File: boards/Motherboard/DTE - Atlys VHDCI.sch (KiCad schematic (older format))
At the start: 3 parts, among them J201 DIGILENT_VHDCI_CONN

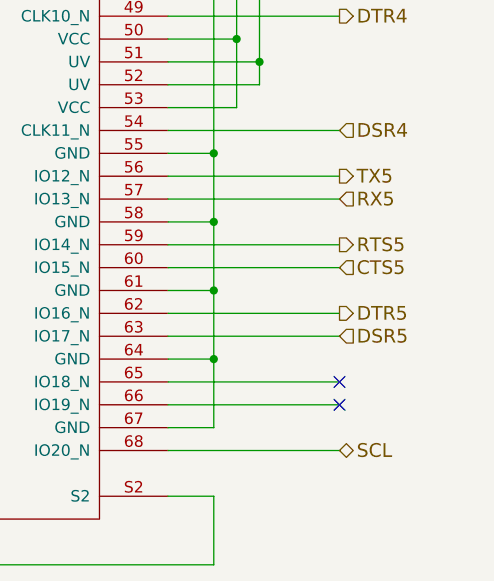
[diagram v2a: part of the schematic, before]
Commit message: Change to 5 serial port; Connect Atlys and PIC18F SPI; Entire schematic updated
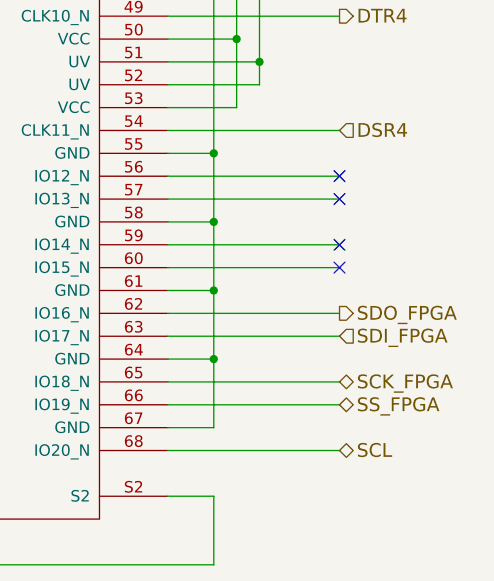
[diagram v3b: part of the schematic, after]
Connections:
- net SCK_FPGA: now reaches J201.65 (IO18_N)
- net SS_FPGA: now reaches J201.66 (IO19_N)
- net CTS5: no longer names the net of J201.60 (IO15_N)
- net DSR5 renamed SDI_FPGA
- net DTR5 renamed SDO_FPGA
- net RTS5: no longer names the net of J201.59 (IO14_N)
- net RX5: no longer names the net of J201.57 (IO13_N)
- net TX5: no longer names the net of J201.56 (IO12_N)
- no-connect marks 2 -> 4
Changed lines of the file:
@@
 Sheet 2 7
 Title ""
-Date "26 jun 2014"
+Date "30 jun 2014"
 Rev ""
 Comp "TimVideos"
@@
 Text HLabel 7350 4150 2    60   Input ~ 0
 DSR4
-Text HLabel 7350 4350 2    60   Output ~ 0
-TX5
-Text HLabel 7350 4650 2    60   Output ~ 0
-RTS5
-Text HLabel 7350 4950 2    60   Output ~ 0
-DTR5
 Text HLabel 7350 5550 2    60   BiDi ~ 0
 SCL
 Text HLabel 7350 2450 2    60   Output ~ 0
 RTS3
-Text HLabel 7350 4450 2    60   Input ~ 0
-RX5
-Text HLabel 7350 4750 2    60   Input ~ 0
-CTS5
-Text HLabel 7350 5050 2    60   Input ~ 0
-DSR5
-NoConn ~ 7350 5250
-NoConn ~ 7350 5350
 Wire Wire Line
 	6800 6050 6800 5750
@@
 Connection ~ 3750 6050
 $Comp
-L PWR_FLAG #FLG201
+L PWR_FLAG #FLG01
 U 1 1 53C07D98
 P 3750 5450
-F 0 "#FLG201" H 3750 5545 30  0001 C CNN
+F 0 "#FLG01" H 3750 5545 30  0001 C CNN
 F 1 "PWR_FLAG" H 3750 5630 30  0001 C CNN
 F 2 "" H 3750 5450 60  0000 C CNN
@@
 Text Notes 1900 7250 0    60   ~ 0
 VHDCI connector gives access to FPGA pins on Digilent Atlys FPGA development board
+NoConn ~ 7350 4350
+NoConn ~ 7350 4450
+NoConn ~ 7350 4650
+NoConn ~ 7350 4750
+Text HLabel 7350 5350 2    60   3State ~ 0
+SS_FPGA
+Text HLabel 7350 5250 2    60   3State ~ 0
+SCK_FPGA
+Text HLabel 7350 5050 2    60   Input ~ 0
+SDI_FPGA
+Text HLabel 7350 4950 2    60   Output ~ 0
+SDO_FPGA
 $EndSCHEMATC

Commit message: Change all serial connections to use BUS
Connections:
- net TX0 renamed SERIAL0
- net TX1 renamed SERIAL6
- net TX2 renamed SERIAL12
- net TX3 renamed SERIAL18
- net TX4 renamed SERIAL24
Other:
- moved on the sheet: C201, J201, R201
